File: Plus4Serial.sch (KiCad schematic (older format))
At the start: 11 parts, among them CN1 PLUS4_USERPORT, CN2 DB9_MALE, U1 MC1489, U2 MC1488

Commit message: Fix some errors
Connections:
- net ~cts: now also CN1.K (D1); no longer CN1.B (D0)
- net ~dcd: now also U1.11 (OUT_D)
- net ~dsr: no longer U1.11 (OUT_D)
- net _dcd renamed _~dcd
- no-connect marks 15 -> 17
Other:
- note added: "+4 HAS NO DEDICATED\n~CTS~ PIN, BUT IF YOU\nLOOK AT THE SCHEMATICS,\nIT WAS DUE TO END UP HERE,\nI.E.: WHERE IT WOULD BE\nON THE C64"
- note added: "MMMH... MAYBE RI COULD BE\nCONNECTED TO A DATA PIN\n(OR ~ATTN~?) THROUGH A DIODE?"
- note removed: "+4 HAS NO DEDICATED\n~CTS PIN, HOPEFULLY\nWE CAN USE A DATA PIN"
- note removed: "MMMH... MAYBE RI COULD BE\nCONNECTED TO A DATA PIN\n(OR ~ATTN?) THROUGH A DIODE?"
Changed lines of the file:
@@
 Sheet 1 1
 Title "Plus4Serial"
-Date "2022-02-13"
+Date "2022-09-04"
 Rev "1git"
 Comp "SukkoPera"
@@
 	6635 2105 7115 2105
 Text Label 7115 2805 2    50   ~ 0
-_dcd
+_~dcd
 Text Label 7115 2605 2    50   ~ 0
 _rxd
@@
 NoConn ~ 8635 4570
 Text Label 9185 4670 2    50   ~ 0
-~dsr
+~dcd
 Wire Wire Line
 	8835 4670 9185 4670
@@
 Text Label 9180 2305 2    50   ~ 0
 ~cts
-Text Label 4240 1950 2    50   ~ 0
+Text Label 4240 2650 2    50   ~ 0
 ~cts
 Wire Wire Line
-	3875 1950 4240 1950
-Text Notes 3880 1815 0    50   ~ 0
-+4 HAS NO DEDICATED\n~CTS PIN, HOPEFULLY\nWE CAN USE A DATA PIN
+	3875 2650 4240 2650
+Text Notes 4360 3060 0    50   ~ 0
++4 HAS NO DEDICATED\n~CTS~ PIN, BUT IF YOU\nLOOK AT THE SCHEMATICS,\nIT WAS DUE TO END UP HERE,\nI.E.: WHERE IT WOULD BE\nON THE C64
 Wire Wire Line
 	10655 5980 10740 5980
@@
 NoConn ~ 3875 2350
 NoConn ~ 3875 2550
-NoConn ~ 3875 2650
 Text Notes 6805 1990 0    50   ~ 0
-MMMH... MAYBE RI COULD BE\nCONNECTED TO A DATA PIN\n(OR ~ATTN?) THROUGH A DIODE?
+MMMH... MAYBE RI COULD BE\nCONNECTED TO A DATA PIN\n(OR ~ATTN~?) THROUGH A DIODE?
+NoConn ~ 3875 1950
+NoConn ~ 8635 3620
+NoConn ~ 1600 2550
+$Comp
+L power:PWR_FLAG #FLG0101
+U 1 1 639336B5
+P 800 7445
+F 0 "#FLG0101" H 800 7520 50  0001 C CNN
+F 1 "PWR_FLAG" H 800 7618 50  0000 C CNN
+F 2 "" H 800 7445 50  0001 C CNN
+F 3 "~" H 800 7445 50  0001 C CNN
+	1    800  7445
+	-1   0    0    1
+$EndComp
+$Comp
+L power:PWR_FLAG #FLG0102
+U 1 1 63935EC7
+P 1280 7445
+F 0 "#FLG0102" H 1280 7520 50  0001 C CNN
+F 1 "PWR_FLAG" H 1280 7618 50  0000 C CNN
+F 2 "" H 1280 7445 50  0001 C CNN
+F 3 "~" H 1280 7445 50  0001 C CNN
+	1    1280 7445
+	-1   0    0    1
+$EndComp
+Wire Wire Line
+	800  7445 800  7350
+Wire Wire Line
+	1280 7445 1280 7350
+$Comp
+L power:+12V #PWR0101
+U 1 1 6393B788
+P 800 7350
+F 0 "#PWR0101" H 800 7200 50  0001 C CNN
+F 1 "+12V" H 815 7523 50  0000 C CNN
+F 2 "" H 800 7350 50  0001 C CNN
+F 3 "" H 800 7350 50  0001 C CNN
+	1    800  7350
+	1    0    0    -1
+$EndComp
+$Comp
+L power:-12V #PWR0102
+U 1 1 6393BFB5
+P 1280 7350
+F 0 "#PWR0102" H 1280 7450 50  0001 C CNN
+F 1 "-12V" H 1295 7523 50  0000 C CNN
+F 2 "" H 1280 7350 50  0001 C CNN
+F 3 "" H 1280 7350 50  0001 C CNN
+	1    1280 7350
+	1    0    0    -1
+$EndComp
 $EndSCHEMATC

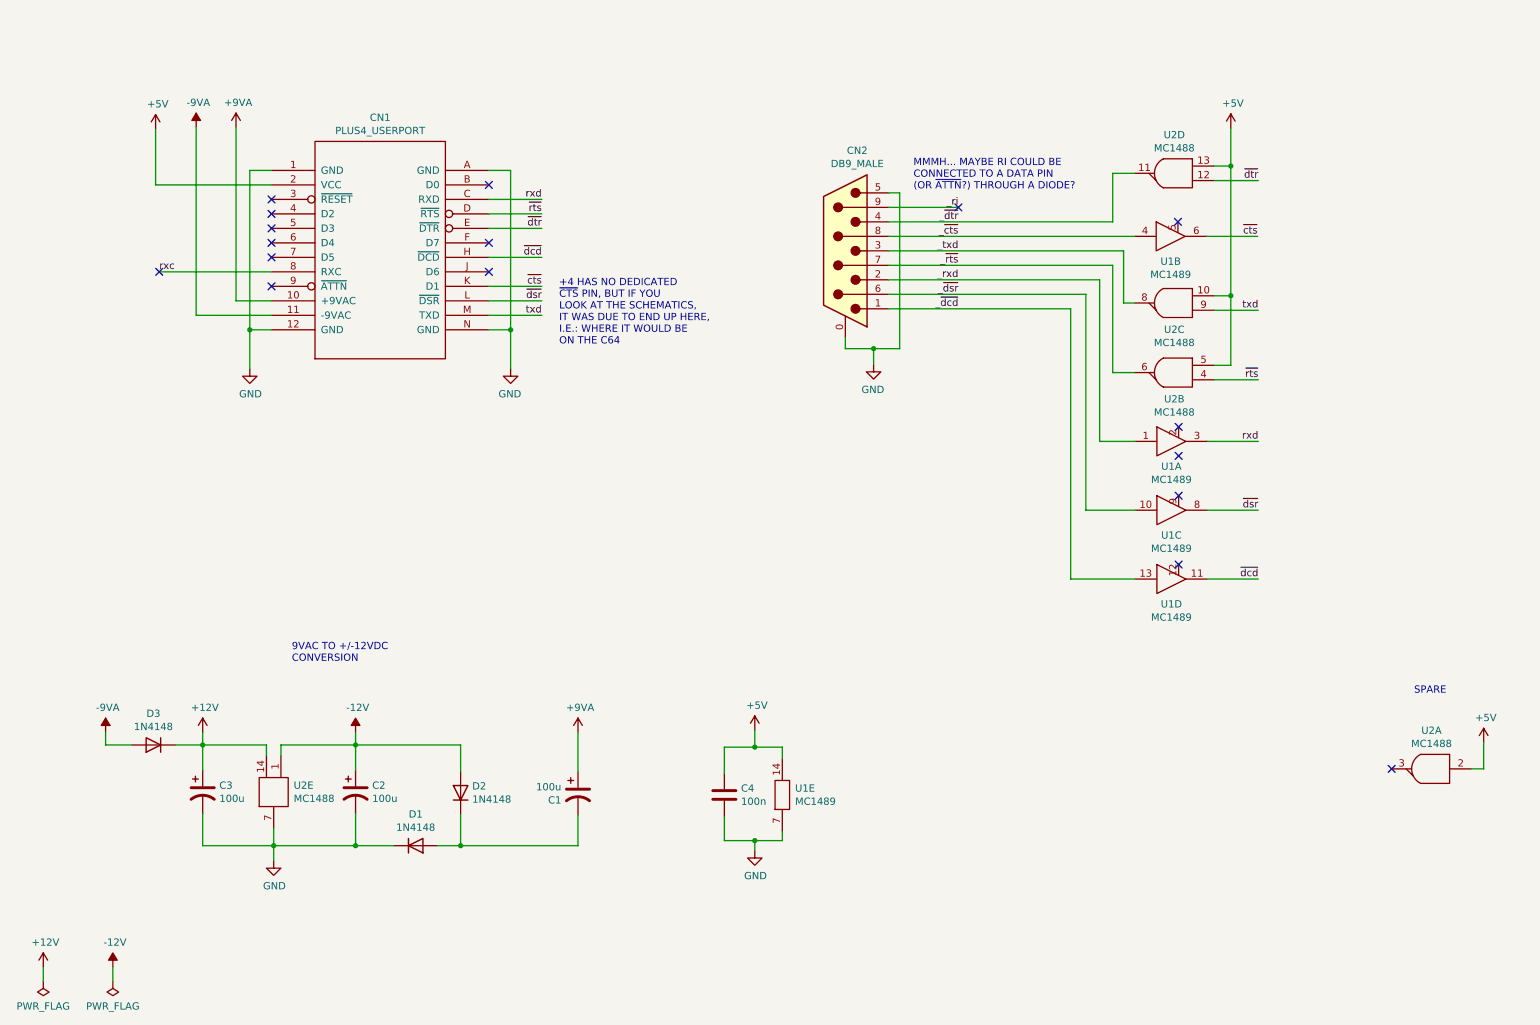
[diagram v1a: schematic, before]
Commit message: Invert signals as per Commodore standard NOTE: PCB not yet updated!
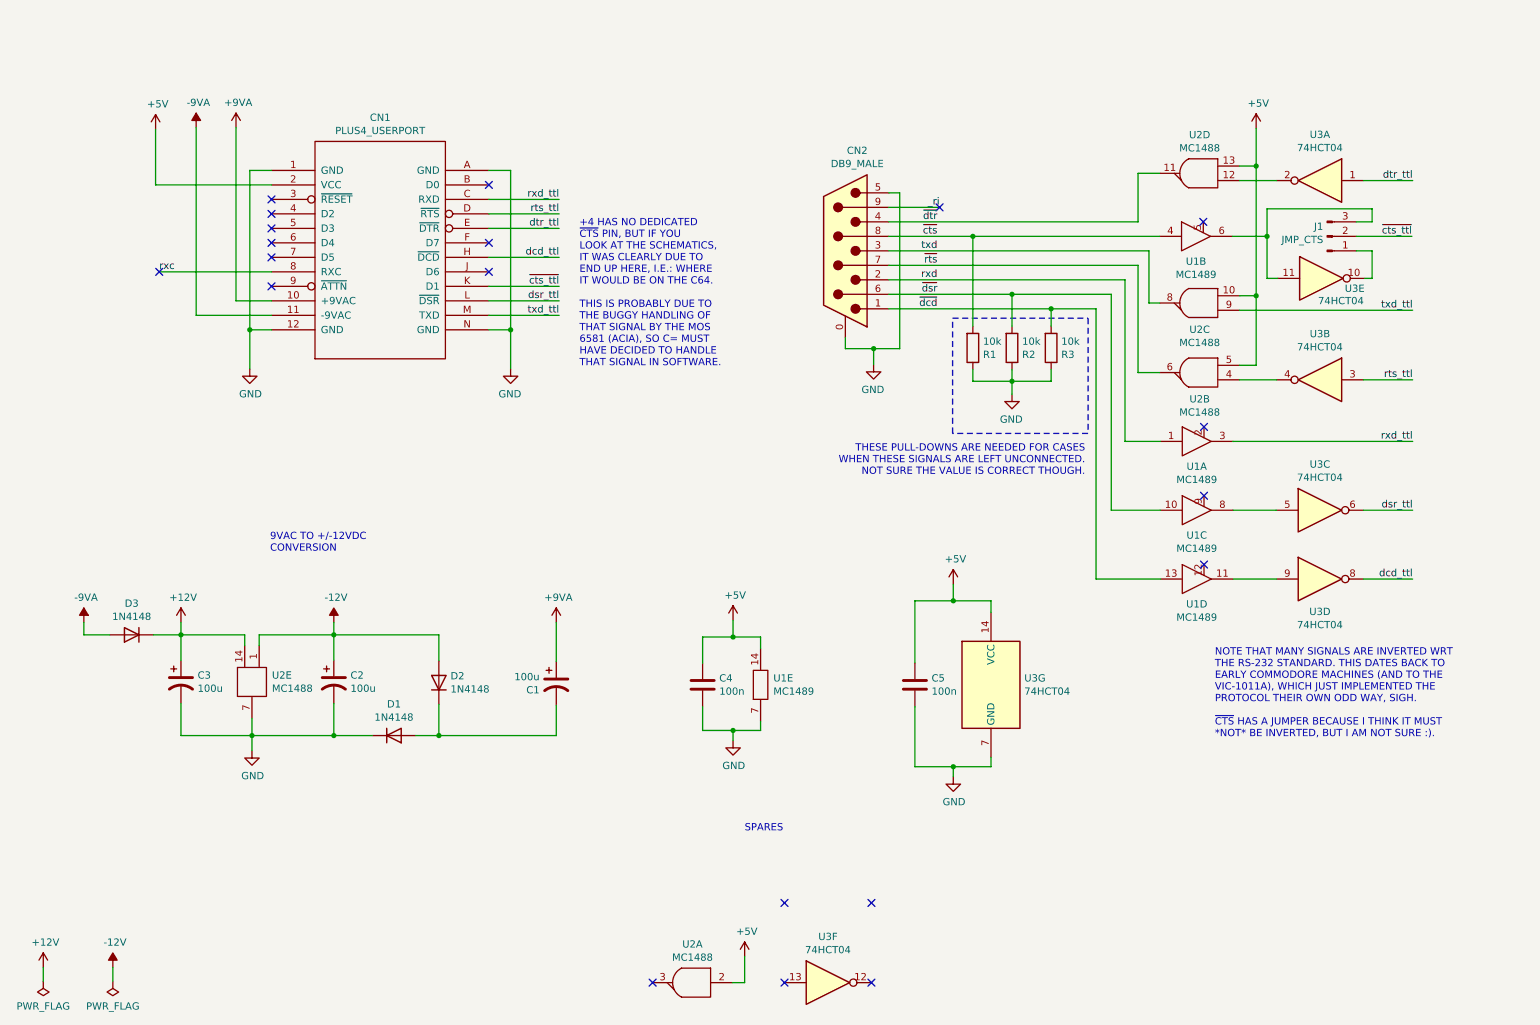
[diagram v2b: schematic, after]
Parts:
- added C5: 100n, Capacitor_THT:C_Disc_D7.0mm_W2.5mm_P5.00mm, symbol Device:C
- added J1: JMP_CTS, Connector_PinHeader_2.54mm:PinHeader_1x03_P2.54mm_Vertical, symbol Connector:Conn_01x03_Male
- added R1, R2, R3: 10k, Resistor_THT:R_Axial_DIN0207_L6.3mm_D2.5mm_P10.16mm_Horizontal, symbol Device:R
- added U3: 74HCT04, Package_DIP:DIP-14_W7.62mm_Socket_LongPads, symbol 74xx:74HCT04
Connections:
- net _rxd is gone; now on net rxd: CN2.2, U1.1 (IN_A)
- net _txd is gone; now on net txd: CN2.3, U2.8 (OUT_C)
- net _~cts is gone; now on net ~cts: CN2.8, U1.4 (IN_B)
- net _~dcd is gone; now on net ~dcd: CN2.1, U1.13 (IN_D)
- net _~dsr is gone; now on net ~dsr: CN2.6, U1.10 (IN_C)
- net _~dtr is gone; now on net ~dtr: CN2.4, U2.11 (OUT_D)
- net _~rts is gone; now on net ~rts: CN2.7, U2.6 (OUT_B)
- net +5V: now also C5.1, U3.14 (VCC)
- net GND: now also C5.2, R1.1, R2.1, R3.1, U3.7 (GND)
- net rxd: no longer CN1.C (RXD), U1.3 (OUT_A)
- net txd: no longer CN1.M (TXD), U2.9 (IN2_C)
- net ~cts: now also R1.2; no longer CN1.K (D1), U1.6 (OUT_B)
- net ~dcd: now also R3.2; no longer CN1.H (~DCD), U1.11 (OUT_D)
- net ~dsr: now also R2.2; no longer CN1.L (~DSR), U1.8 (OUT_C)
- net ~dtr: no longer CN1.E (~DTR), U2.12 (IN2_D)
- net ~rts: no longer CN1.D (~RTS), U2.4 (IN1_B)
- new net: U2.12 (IN2_D), U3.2
- new net: U2.4 (IN1_B), U3.4
- new net: U1.8 (OUT_C), U3.5
- new net: U1.11 (OUT_D), U3.9
- new net: J1.1 (Pin_1), U3.10
- new net: J1.3 (Pin_3), U1.6 (OUT_B), U3.11
- new net dcd_ttl: CN1.H (~DCD), U3.8
- new net dsr_ttl: CN1.L (~DSR), U3.6
- new net dtr_ttl: CN1.E (~DTR), U3.1
- new net rts_ttl: CN1.D (~RTS), U3.3
- new net rxd_ttl: CN1.C (RXD), U1.3 (OUT_A)
- new net txd_ttl: CN1.M (TXD), U2.9 (IN2_C)
- new net ~cts_ttl: CN1.K (D1), J1.2 (Pin_2)
- no-connect marks 17 -> 20
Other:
- note added: "+4 HAS NO DEDICATED\n~CTS~ PIN, BUT IF YOU\nLOOK AT THE SCHEMATICS,\nIT WAS CLEARLY DUE TO\nEND UP HERE, I.E.: WHERE\nIT WOULD BE ON THE C64.\n\nTHIS IS PROBABLY DUE TO\nTHE BUGGY HANDLING OF\nTHAT SIGNAL BY THE MOS\n6581 (ACIA), SO C= MUST\nHAVE DECIDED TO HANDLE\nTHAT SIGNAL IN SOFTWARE."
- note added: "NOTE THAT MANY SIGNALS ARE INVERTED WRT\nTHE RS-232 STANDARD. THIS DATES BACK TO\nEARLY COMMODORE MACHINES (AND TO THE\nVIC-1011A), WHICH JUST IMPLEMENTED THE\nPROTOCOL THEIR OWN ODD WAY, SIGH.\n\n~CTS~ HAS A JUMPER BECAUSE I THINK IT MUST\n*NOT* BE INVERTED, BUT I AM NOT SURE :)."
- note added: "SPARES"
- note added: "THESE PULL-DOWNS ARE NEEDED FOR CASES\nWHEN THESE SIGNALS ARE LEFT UNCONNECTED.\nNOT SURE THE VALUE IS CORRECT THOUGH."
- note removed: "+4 HAS NO DEDICATED\n~CTS~ PIN, BUT IF YOU\nLOOK AT THE SCHEMATICS,\nIT WAS DUE TO END UP HERE,\nI.E.: WHERE IT WOULD BE\nON THE C64"
- note removed: "MMMH... MAYBE RI COULD BE\nCONNECTED TO A DATA PIN\n(OR ~ATTN~?) THROUGH A DIODE?"
- note removed: "SPARE"
- moved on the sheet: C1, C2, C3, C4, D1, D2, D3, U1A, U1B, U1C, U1D, U1E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

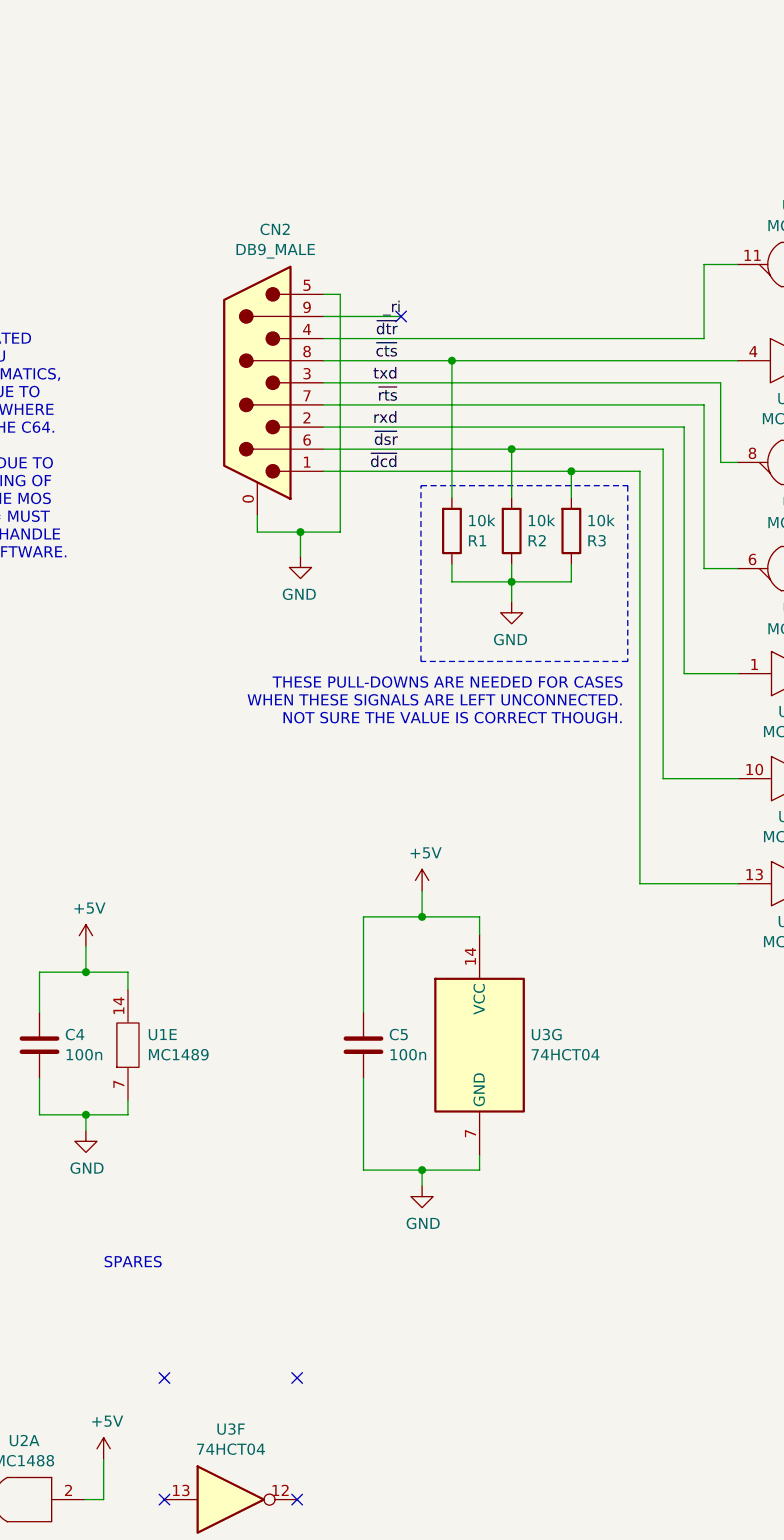
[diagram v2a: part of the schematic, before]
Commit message: Erm, fix pull-UPs
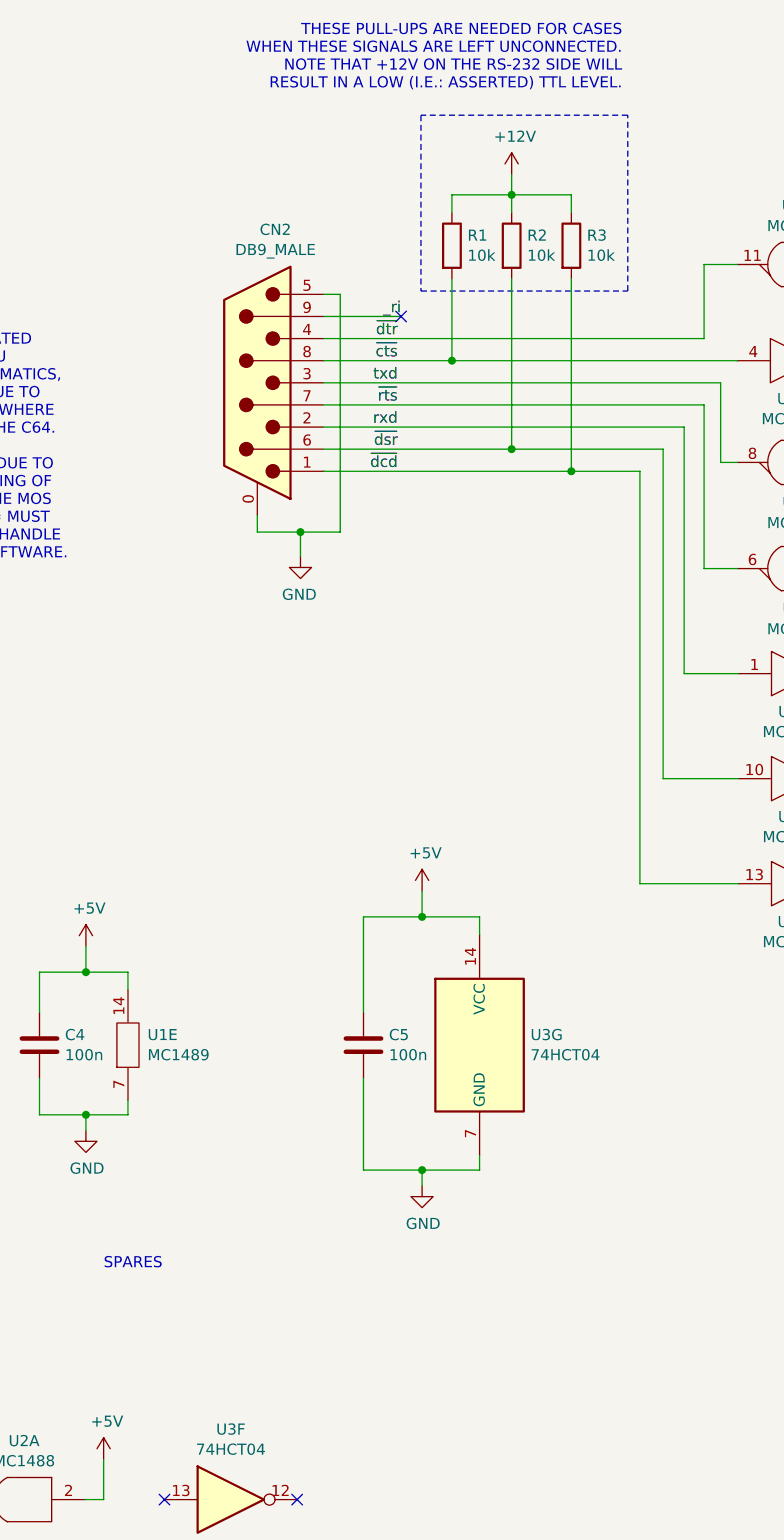
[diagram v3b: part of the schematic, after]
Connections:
- net +12V: now also R1.1, R2.1, R3.1
- net GND: no longer R1.1, R2.1, R3.1
- no-connect marks 20 -> 18
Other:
- note added: "THESE PULL-UPS ARE NEEDED FOR CASES\nWHEN THESE SIGNALS ARE LEFT UNCONNECTED.\nNOTE THAT +12V ON THE RS-232 SIDE WILL\nRESULT IN A LOW (I.E.: ASSERTED) TTL LEVEL."
- note removed: "THESE PULL-DOWNS ARE NEEDED FOR CASES\nWHEN THESE SIGNALS ARE LEFT UNCONNECTED.\nNOT SURE THE VALUE IS CORRECT THOUGH."
- moved on the sheet: R1, R2, R3
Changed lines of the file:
@@
 	1    0    0    -1
 $EndComp
-NoConn ~ 5915 6905
-NoConn ~ 6515 6905
 NoConn ~ 5915 7455
 NoConn ~ 6515 7455
@@
 L Device:R R1
 U 1 1 633ED6A2
-P 7215 3075
-F 0 "R1" H 7285 3121 50  0000 L CNN
-F 1 "10k" H 7285 3030 50  0000 L CNN
-F 2 "Resistor_THT:R_Axial_DIN0207_L6.3mm_D2.5mm_P10.16mm_Horizontal" V 7145 3075 50  0001 C CNN
-F 3 "~" H 7215 3075 50  0001 C CNN
-	1    7215 3075
-	1    0    0    1
+P 7215 1785
+F 0 "R1" H 7285 1831 50  0000 L CNN
+F 1 "10k" H 7285 1740 50  0000 L CNN
+F 2 "Resistor_THT:R_Axial_DIN0207_L6.3mm_D2.5mm_P10.16mm_Horizontal" V 7145 1785 50  0001 C CNN
+F 3 "~" H 7215 1785 50  0001 C CNN
+	1    7215 1785
+	1    0    0    -1
 $EndComp
 $Comp
 L Device:R R2
 U 1 1 633ED7A2
-P 7485 3075
-F 0 "R2" H 7555 3121 50  0000 L CNN
-F 1 "10k" H 7555 3030 50  0000 L CNN
-F 2 "Resistor_THT:R_Axial_DIN0207_L6.3mm_D2.5mm_P10.16mm_Horizontal" V 7415 3075 50  0001 C CNN
-F 3 "~" H 7485 3075 50  0001 C CNN
-	1    7485 3075
-	1    0    0    1
+P 7485 1785
+F 0 "R2" H 7555 1831 50  0000 L CNN
+F 1 "10k" H 7555 1740 50  0000 L CNN
+F 2 "Resistor_THT:R_Axial_DIN0207_L6.3mm_D2.5mm_P10.16mm_Horizontal" V 7415 1785 50  0001 C CNN
+F 3 "~" H 7485 1785 50  0001 C CNN
+	1    7485 1785
+	1    0    0    -1
 $EndComp
 $Comp
 L Device:R R3
 U 1 1 633FDE96
-P 7755 3075
-F 0 "R3" H 7825 3121 50  0000 L CNN
-F 1 "10k" H 7825 3030 50  0000 L CNN
-F 2 "Resistor_THT:R_Axial_DIN0207_L6.3mm_D2.5mm_P10.16mm_Horizontal" V 7685 3075 50  0001 C CNN
-F 3 "~" H 7755 3075 50  0001 C CNN
-	1    7755 3075
-	1    0    0    1
-$EndComp
-Wire Wire Line
-	7215 3225 7215 3305
-Wire Wire Line
-	7215 3305 7485 3305
-Wire Wire Line
-	7755 3305 7755 3225
-Wire Wire Line
-	7485 3225 7485 3305
-Connection ~ 7485 3305
-Wire Wire Line
-	7485 3305 7755 3305
-Wire Wire Line
-	7485 3305 7485 3395
+P 7755 1785
+F 0 "R3" H 7825 1831 50  0000 L CNN
+F 1 "10k" H 7825 1740 50  0000 L CNN
+F 2 "Resistor_THT:R_Axial_DIN0207_L6.3mm_D2.5mm_P10.16mm_Horizontal" V 7685 1785 50  0001 C CNN
+F 3 "~" H 7755 1785 50  0001 C CNN
+	1    7755 1785
+	1    0    0    -1
+$EndComp
+Wire Wire Line
+	7215 1635 7215 1555
+Wire Wire Line
+	7215 1555 7485 1555
+Wire Wire Line
+	7755 1555 7755 1635
+Wire Wire Line
+	7485 1635 7485 1555
+Connection ~ 7485 1555
+Wire Wire Line
+	7485 1555 7755 1555
+Wire Wire Line
+	7485 1555 7485 1465
 $Comp
 L mc1488:MC1488 U2
@@
 	6635 2205 8355 2205
 Wire Wire Line
-	6635 2705 7485 2705
-Wire Wire Line
-	6635 2805 7755 2805
-Wire Wire Line
 	6635 2505 8355 2505
 Wire Wire Line
@@
 Wire Wire Line
 	6635 2305 7215 2305
-Wire Wire Line
-	7215 2305 7215 2925
 Connection ~ 7215 2305
 Wire Wire Line
 	7215 2305 8505 2305
-Wire Wire Line
-	7485 2705 7485 2925
-Connection ~ 7485 2705
-Wire Wire Line
-	7485 2705 8170 2705
-Wire Wire Line
-	7755 2925 7755 2805
-Connection ~ 7755 2805
-Wire Wire Line
-	7755 2805 8065 2805
-$Comp
-L power:GND #PWR018
-U 1 1 6349FF29
-P 7485 3395
-F 0 "#PWR018" H 7485 3145 50  0001 C CNN
-F 1 "GND" H 7490 3222 50  0000 C CNN
-F 2 "" H 7485 3395 50  0001 C CNN
-F 3 "" H 7485 3395 50  0001 C CNN
-	1    7485 3395
-	-1   0    0    -1
-$EndComp
 Wire Notes Line
-	7075 2870 8010 2870
+	7075 1990 8010 1990
 Wire Notes Line
-	8010 2870 8010 3665
+	8010 1990 8010 1195
 Wire Notes Line
-	8010 3665 7075 3665
+	8010 1195 7075 1195
 Wire Notes Line
-	7075 3665 7075 2870
-Text Notes 7990 3960 2    50   ~ 0
-THESE PULL-DOWNS ARE NEEDED FOR CASES\nWHEN THESE SIGNALS ARE LEFT UNCONNECTED.\nNOT SURE THE VALUE IS CORRECT THOUGH.
+	7075 1195 7075 1990
+Text Notes 7985 1085 2    50   ~ 0
+THESE PULL-UPS ARE NEEDED FOR CASES\nWHEN THESE SIGNALS ARE LEFT UNCONNECTED.\nNOTE THAT +12V ON THE RS-232 SIDE WILL\nRESULT IN A LOW (I.E.: ASSERTED) TTL LEVEL.
 $Comp
 L Connector:Conn_01x03_Male J1
@@
 Wire Wire Line
 	9005 2305 9245 2305
+Wire Wire Line
+	7215 2305 7215 1935
+Wire Wire Line
+	6635 2705 7485 2705
+Wire Wire Line
+	6635 2805 7755 2805
+Wire Wire Line
+	7485 1935 7485 2705
+Connection ~ 7485 2705
+Wire Wire Line
+	7485 2705 8170 2705
+Wire Wire Line
+	7755 1935 7755 2805
+Connection ~ 7755 2805
+Wire Wire Line
+	7755 2805 8065 2805
+$Comp
+L power:+12V #PWR?
+U 1 1 6352CF44
+P 7485 1465
+F 0 "#PWR?" H 7485 1315 50  0001 C CNN
+F 1 "+12V" H 7500 1638 50  0000 C CNN
+F 2 "" H 7485 1465 50  0001 C CNN
+F 3 "" H 7485 1465 50  0001 C CNN
+	1    7485 1465
+	1    0    0    -1
+$EndComp
 $EndSCHEMATC
